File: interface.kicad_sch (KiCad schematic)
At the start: 18 parts

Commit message: 回路設計済
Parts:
- removed Q?: BSS138, symbol Device:Q_NMOS_DGS
- added Q2: BSS138, Package_TO_SOT_SMD:SOT-23, symbol Transistor_FET:BSS138
- C10, C9: renamed from C?; footprint (none) -> Capacitor_SMD:C_0603_1608Metric_Pad1.08x0.95mm_HandSolder
- D2, D3, D4, D5: renamed from D?; footprint (none) -> LED_SMD:LED_0603_1608Metric_Pad1.05x0.95mm_HandSolder
- J10: renamed from J?; footprint (none) -> Connector_PinHeader_2.54mm:PinHeader_1x04_P2.54mm_Horizontal
- J11: renamed from J?; footprint (none) -> Connector_JST:JST_SH_BM04B-SRSS-TB_1x04-1MP_P1.00mm_Vertical
- LS1: renamed from LS?; footprint (none) -> omni:STM0440-T-R
- R10, R11, R6, R7, R8, R9: renamed from R?; footprint (none) -> Resistor_SMD:R_0805_2012Metric_Pad1.20x1.40mm_HandSolder
- SW: renamed from SW?; footprint (none) -> Button_Switch_SMD:SW_Push_1P1T_NO_Vertical_Wuerth_434133025816
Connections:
- net BUZZER_INPUT: now also Q2.1 (G)
- net GND: now also Q2.2 (S)
- net at LS1.2: now also Q2.3 (D)

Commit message: update pcb
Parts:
- removed unit 2 of SW
- added SW3: SKRPACE, Button_Switch_SMD:SW_Push_1P1T_NO_Vertical_Wuerth_434133025816, symbol Switch:SW_Push_Dual_x2
- J10: footprint Connector_PinHeader_2.54mm:PinHeader_1x04_P2.54mm_Horizontal -> Connector_PinHeader_2.54mm:PinHeader_1x04_P2.54mm_Vertical
- J11: footprint Connector_JST:JST_SH_BM04B-SRSS-TB_1x04-1MP_P1.00mm_Vertical -> Connector_JST:JST_SH_SM04B-SRSS-TB_1x04-1MP_P1.00mm_Horizontal
- renumbered SW to SW2
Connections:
- net BUTTON_OUTPUT: now also SW3.2 (D)
- net GND: now also SW3.1 (C)
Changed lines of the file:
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@@
     (pin "2")
-  )
-  (symbol (lib_id "Switch:SW_Push_Dual_x2") (at 173.99 97.79 90) (unit 2)
-    (in_bom yes) (on_board yes)
-    (property "Reference" "SW" (id 0) (at 175.26 99.0599 90)
-      (effects (font (size 1.27 1.27)) (justify right))
-    )
-    (property "Value" "SKRPACE" (id 1) (at 175.26 101.5999 90)
-      (effects (font (size 1.27 1.27)) (justify right))
-    )
-    (property "Footprint" "Button_Switch_SMD:SW_Push_1P1T_NO_Vertical_Wuerth_434133025816" (id 2) (at 168.91 97.79 0)
-      (effects (font (size 1.27 1.27)) hide)
-    )
-    (property "Datasheet" "~" (id 3) (at 168.91 97.79 0)
-      (effects (font (size 1.27 1.27)) hide)
-    )
-    (pin "1")
-    (pin "2")
-    (pin "3")
-    (pin "4")
   )
   (symbol (lib_id "Device:LED") (at 82.55 60.96 90) (unit 1)
@@
   (symbol (lib_id "Switch:SW_Push_Dual_x2") (at 147.32 95.25 90) (unit 1)
     (in_bom yes) (on_board yes)
-    (property "Reference" "SW" (id 0) (at 148.59 97.7899 90)
+    (property "Reference" "SW2" (id 0) (at 148.59 97.7899 90)
       (effects (font (size 1.27 1.27)) (justify right))
     )
@@
       (effects (font (size 1.27 1.27)) (justify left))
     )
-    (property "Footprint" "Connector_JST:JST_SH_BM04B-SRSS-TB_1x04-1MP_P1.00mm_Vertical" (id 2) (at 168.91 59.69 0)
+    (property "Footprint" "Connector_JST:JST_SH_SM04B-SRSS-TB_1x04-1MP_P1.00mm_Horizontal" (id 2) (at 168.91 59.69 0)
       (effects (font (size 1.27 1.27)) hide)
     )
     (property "Datasheet" "~" (id 3) (at 168.91 59.69 0)
+      (effects (font (size 1.27 1.27)) hide)
+    )
+    (pin "1")
+    (pin "2")
+    (pin "3")
+    (pin "4")
+  )
+  (symbol (lib_id "Switch:SW_Push_Dual_x2") (at 173.99 97.79 90) (unit 1)
+    (in_bom yes) (on_board yes)
+    (property "Reference" "SW3" (id 0) (at 175.26 100.3299 90)
+      (effects (font (size 1.27 1.27)) (justify right))
+    )
+    (property "Value" "SKRPACE" (id 1) (at 175.26 102.8699 90)
+      (effects (font (size 1.27 1.27)) (justify right))
+    )
+    (property "Footprint" "Button_Switch_SMD:SW_Push_1P1T_NO_Vertical_Wuerth_434133025816" (id 2) (at 168.91 97.79 0)
+      (effects (font (size 1.27 1.27)) hide)
+    )
+    (property "Datasheet" "~" (id 3) (at 168.91 97.79 0)
       (effects (font (size 1.27 1.27)) hide)
     )
@@
       (effects (font (size 1.27 1.27)) (justify left))
     )
-    (property "Footprint" "Connector_PinHeader_2.54mm:PinHeader_1x04_P2.54mm_Horizontal" (id 2) (at 128.27 59.69 0)
-      (effects (font (size 1.27 1.27)) hide)
-    )
+    (property "Footprint" "Connector_PinHeader_2.54mm:PinHeader_1x04_P2.54mm_Vertical" (id 2) (at 128.27 59.69 0)
+      (effects (font (size 1.27 1.27)) hide)
+    )

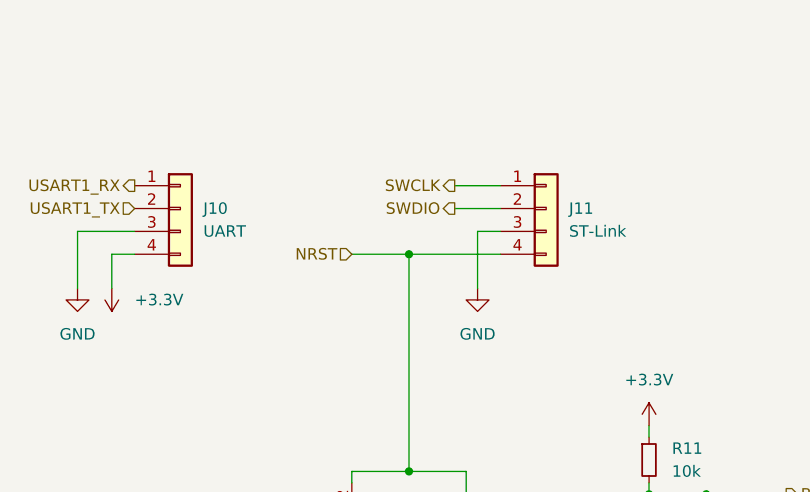
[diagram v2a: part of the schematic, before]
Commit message: 部品配置完了
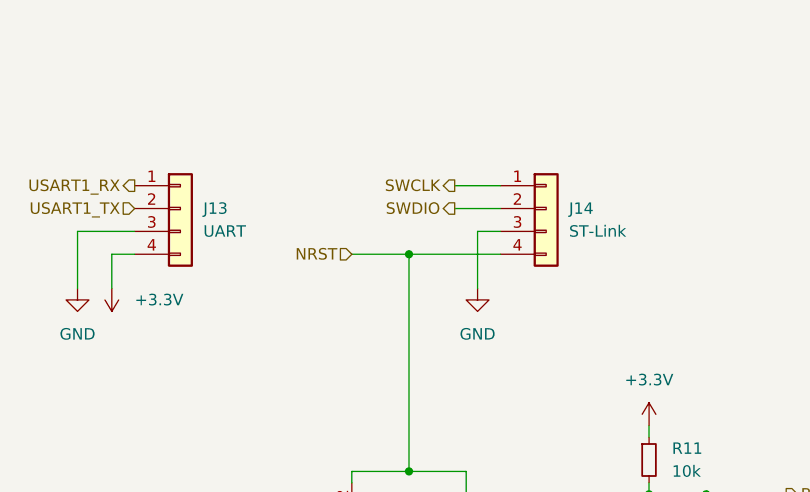
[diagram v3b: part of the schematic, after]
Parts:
- renumbered J10 to J13, J11 to J14
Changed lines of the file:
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@@
   (symbol (lib_id "power:GND") (at 161.29 68.58 0) (unit 1)
     (in_bom yes) (on_board yes) (fields_autoplaced)
-    (property "Reference" "#PWR076" (id 0) (at 161.29 74.93 0)
+    (property "Reference" "#PWR024" (id 0) (at 161.29 74.93 0)
       (effects (font (size 1.27 1.27)) hide)
     )
@@
   (symbol (lib_id "power:GND") (at 73.66 130.81 0) (unit 1)
     (in_bom yes) (on_board yes) (fields_autoplaced)
-    (property "Reference" "#PWR071" (id 0) (at 73.66 137.16 0)
+    (property "Reference" "#PWR019" (id 0) (at 73.66 137.16 0)
       (effects (font (size 1.27 1.27)) hide)
     )
@@
   (symbol (lib_id "power:GND") (at 63.5 68.58 0) (unit 1)
     (in_bom yes) (on_board yes) (fields_autoplaced)
-    (property "Reference" "#PWR068" (id 0) (at 63.5 74.93 0)
+    (property "Reference" "#PWR016" (id 0) (at 63.5 74.93 0)
       (effects (font (size 1.27 1.27)) hide)
     )
@@
   (symbol (lib_id "power:+3.3V") (at 120.65 68.58 180) (unit 1)
     (in_bom yes) (on_board yes) (fields_autoplaced)
-    (property "Reference" "#PWR074" (id 0) (at 120.65 64.77 0)
+    (property "Reference" "#PWR022" (id 0) (at 120.65 64.77 0)
       (effects (font (size 1.27 1.27)) hide)
     )
@@
   (symbol (lib_id "power:GND") (at 116.84 68.58 0) (unit 1)
     (in_bom yes) (on_board yes) (fields_autoplaced)
-    (property "Reference" "#PWR073" (id 0) (at 116.84 74.93 0)
+    (property "Reference" "#PWR021" (id 0) (at 116.84 74.93 0)
       (effects (font (size 1.27 1.27)) hide)
     )
@@
   (symbol (lib_id "power:GND") (at 82.55 68.58 0) (unit 1)
     (in_bom yes) (on_board yes) (fields_autoplaced)
-    (property "Reference" "#PWR072" (id 0) (at 82.55 74.93 0)
+    (property "Reference" "#PWR020" (id 0) (at 82.55 74.93 0)
       (effects (font (size 1.27 1.27)) hide)
     )
@@
   (symbol (lib_id "power:GND") (at 153.67 106.68 0) (unit 1)
     (in_bom yes) (on_board yes) (fields_autoplaced)
-    (property "Reference" "#PWR075" (id 0) (at 153.67 113.03 0)
+    (property "Reference" "#PWR023" (id 0) (at 153.67 113.03 0)
       (effects (font (size 1.27 1.27)) hide)
     )
@@
   (symbol (lib_id "power:+3.3V") (at 180.34 83.82 0) (unit 1)
     (in_bom yes) (on_board yes)
-    (property "Reference" "#PWR077" (id 0) (at 180.34 87.63 0)
+    (property "Reference" "#PWR025" (id 0) (at 180.34 87.63 0)
       (effects (font (size 1.27 1.27)) hide)
     )
@@
   (symbol (lib_id "power:+3.3V") (at 73.66 102.87 0) (unit 1)
     (in_bom yes) (on_board yes) (fields_autoplaced)
-    (property "Reference" "#PWR070" (id 0) (at 73.66 106.68 0)
+    (property "Reference" "#PWR018" (id 0) (at 73.66 106.68 0)
       (effects (font (size 1.27 1.27)) hide)
     )
@@
   (symbol (lib_id "power:GND") (at 180.34 106.68 0) (unit 1)
     (in_bom yes) (on_board yes) (fields_autoplaced)
-    (property "Reference" "#PWR078" (id 0) (at 180.34 113.03 0)
+    (property "Reference" "#PWR026" (id 0) (at 180.34 113.03 0)
       (effects (font (size 1.27 1.27)) hide)
     )
@@
   (symbol (lib_id "power:GND") (at 72.39 68.58 0) (unit 1)
     (in_bom yes) (on_board yes) (fields_autoplaced)
-    (property "Reference" "#PWR069" (id 0) (at 72.39 74.93 0)
+    (property "Reference" "#PWR017" (id 0) (at 72.39 74.93 0)
       (effects (font (size 1.27 1.27)) hide)
     )
@@
   (symbol (lib_id "power:GND") (at 54.61 68.58 0) (unit 1)
     (in_bom yes) (on_board yes) (fields_autoplaced)
-    (property "Reference" "#PWR067" (id 0) (at 54.61 74.93 0)
+    (property "Reference" "#PWR015" (id 0) (at 54.61 74.93 0)
       (effects (font (size 1.27 1.27)) hide)
     )
@@
   (symbol (lib_id "Connector_Generic:Conn_01x04") (at 168.91 59.69 0) (unit 1)
     (in_bom yes) (on_board yes) (fields_autoplaced)
-    (property "Reference" "J11" (id 0) (at 171.45 59.6899 0)
+    (property "Reference" "J14" (id 0) (at 171.45 59.6899 0)
       (effects (font (size 1.27 1.27)) (justify left))
     )
@@
   (symbol (lib_id "Connector_Generic:Conn_01x04") (at 128.27 59.69 0) (unit 1)
     (in_bom yes) (on_board yes) (fields_autoplaced)
-    (property "Reference" "J10" (id 0) (at 130.81 59.6899 0)
-      (effects (font (size 1.27 1.27)) (justify left))
-    )
+    (property "Reference" "J13" (id 0) (at 130.81 59.6899 0)
+      (effects (font (size 1.27 1.27)) (justify left))
+    )
